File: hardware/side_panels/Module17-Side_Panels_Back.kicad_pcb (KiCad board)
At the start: 2 copper layers, 103 x 30.5 mm, 2 parts

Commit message: Updated HMI
Added JLCPCB placeholder for batch number, removed useless texts
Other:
- board text added: "JLCJLCJLCJLC"
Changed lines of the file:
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@@
     )
+  )
+  (gr_text "JLCJLCJLCJLC" (at 114.375 119.42) (layer "B.SilkS")
+    (effects (font (size 1 1) (thickness 0.1)) (justify mirror))
   )
   (gr_text "Packet radio + CAT" (at 141.385 98.045) (layer "F.SilkS")

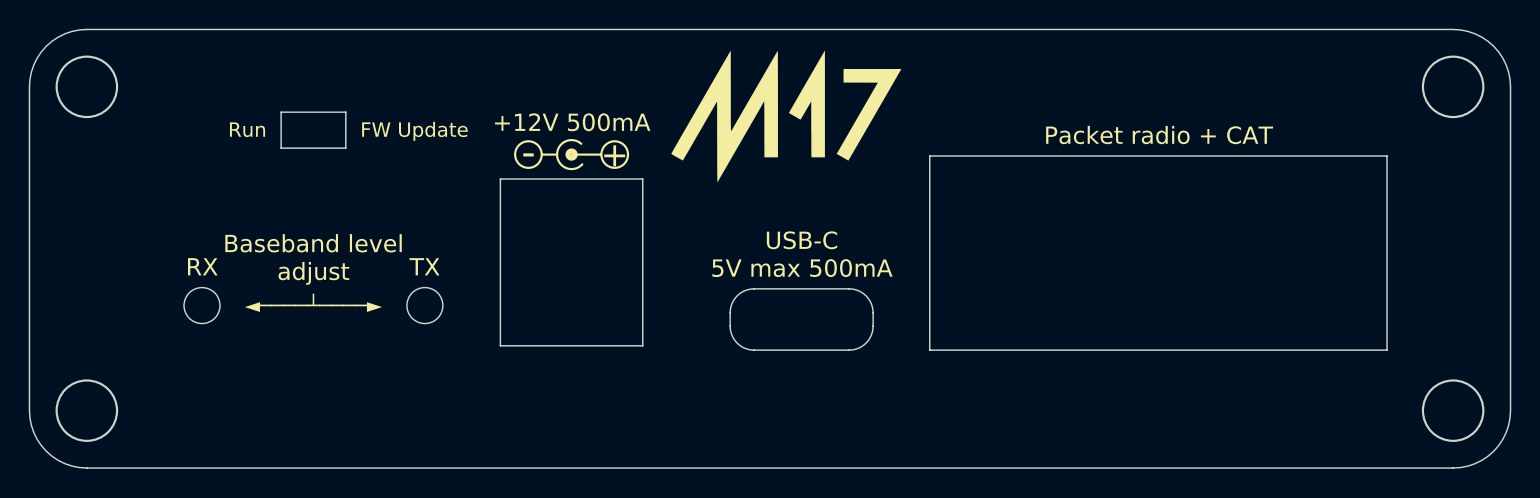
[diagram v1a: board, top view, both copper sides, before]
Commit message: Updated HMI side panels
Increased text size, added holes for the corners, added schematic title bloc plus misc. changes
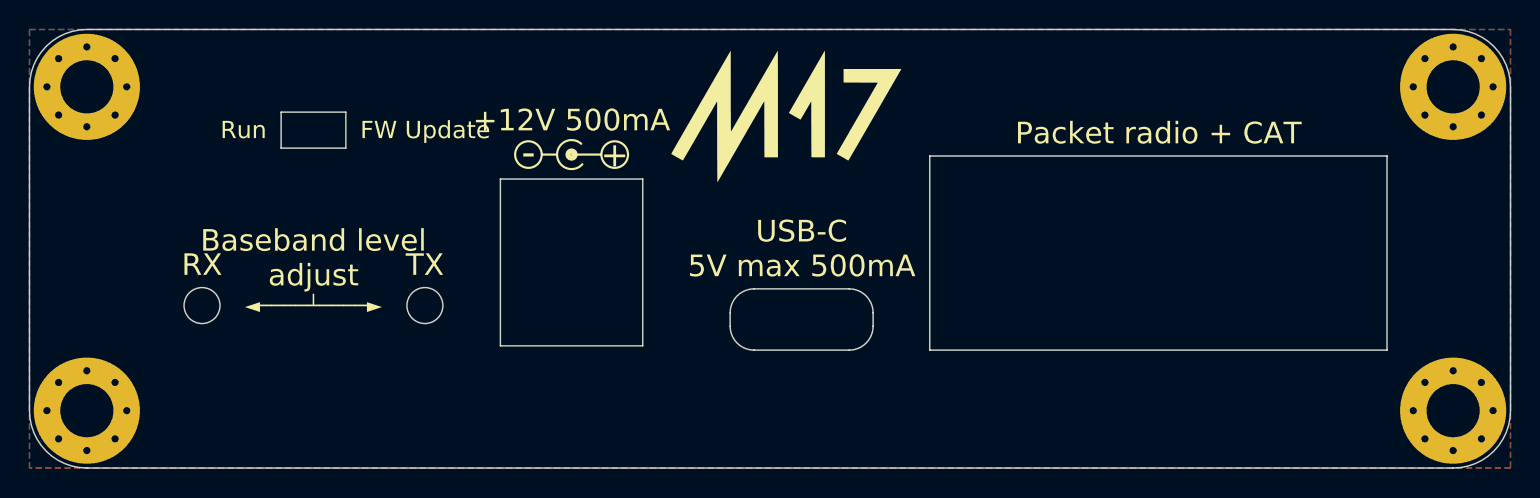
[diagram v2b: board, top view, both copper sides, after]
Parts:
- removed the REF** at (115.5, 96.0)
- added H1: MountingHole_Pad, MountingHole:MountingHole_3.7mm_Pad_Via, F.Cu at (66.9, 93.9)
- added H2: MountingHole_Pad, MountingHole:MountingHole_3.7mm_Pad_Via, F.Cu at (161.9, 93.9)
- added H3: MountingHole_Pad, MountingHole:MountingHole_3.7mm_Pad_Via, F.Cu at (161.9, 116.5)
- added H4: MountingHole_Pad, MountingHole:MountingHole_3.7mm_Pad_Via, F.Cu at (66.9, 116.5)
- added LOGO1: M17_logo, M17_logos:M17_logo_16x9.2mm, F.Cu at (115.5, 96.0)
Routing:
- added copper zone on B.Cu, net GND
- added copper zone on F.Cu, net GND
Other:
- outline, holes or cut-outs redrawn
